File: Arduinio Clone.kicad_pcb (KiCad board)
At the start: 2 copper layers, 0 parts

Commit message: Added design rules
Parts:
- added BT1: Battery 3V, Connector_PinHeader_2.54mm:PinHeader_1x02_P2.54mm_Vertical, F.Cu at (130.8, 66.0)
- added C1: 220pF, Capacitor_SMD:C_0805_2012Metric, F.Cu at (127.7, 79.5)
- added C2: 220pF, Capacitor_SMD:C_0805_2012Metric, F.Cu at (133.4, 72.4)
- added C3: 10uF, Capacitor_SMD:C_0805_2012Metric, F.Cu at (140.4, 65.2)
- added D1: LED, LED_SMD:LED_0805_2012Metric, F.Cu at (128.9, 72.4)
- added J1: Serial, Connector_PinHeader_2.54mm:PinHeader_1x04_P2.54mm_Vertical, F.Cu at (157.3, 66.0)
- added J2: Digital Pins, Connector_PinHeader_2.54mm:PinHeader_1x09_P2.54mm_Vertical, F.Cu at (148.0, 66.0)
- added J3: ICSP, Connector_PinHeader_2.54mm:PinHeader_2x03_P2.54mm_Vertical, F.Cu at (161.9, 66.0)
- added J4: I2C, Connector_PinHeader_2.54mm:PinHeader_1x04_P2.54mm_Vertical, F.Cu at (152.6, 66.0)
- added R1: 330, Resistor_SMD:R_0805_2012Metric_Pad1.20x1.40mm_HandSolder, F.Cu at (127.9, 76.5)
- added R2: 10k, Resistor_SMD:R_0805_2012Metric_Pad1.20x1.40mm_HandSolder, F.Cu at (135.5, 68.6)
- added U1: DS1337_GM, Package_SO:SO-8_5.3x6.2mm_P1.27mm, F.Cu at (111.8, 79.2)
- added U2: 24LC1025, Package_SO:SOIC-8_3.9x4.9mm_P1.27mm, F.Cu at (122.5, 71.8)
- added U3: ATmega328P-A, Package_QFP:TQFP-32_7x7mm_P0.8mm, F.Cu at (112.4, 69.5)
- added U4: 24LC1025, Package_SO:SOIC-8_3.9x4.9mm_P1.27mm, F.Cu at (121.3, 78.6)
- added Y1: Crystal 32MHz, Crystal:Crystal_SMD_MicroCrystal_CC7V-T1A-2Pin_3.2x1.5mm, F.Cu at (135.7, 65.4)
- added Y2: Crystal 16MHz, Crystal:Crystal_SMD_5032-2Pin_5.0x3.2mm_HandSoldering, F.Cu at (123.4, 66.1)

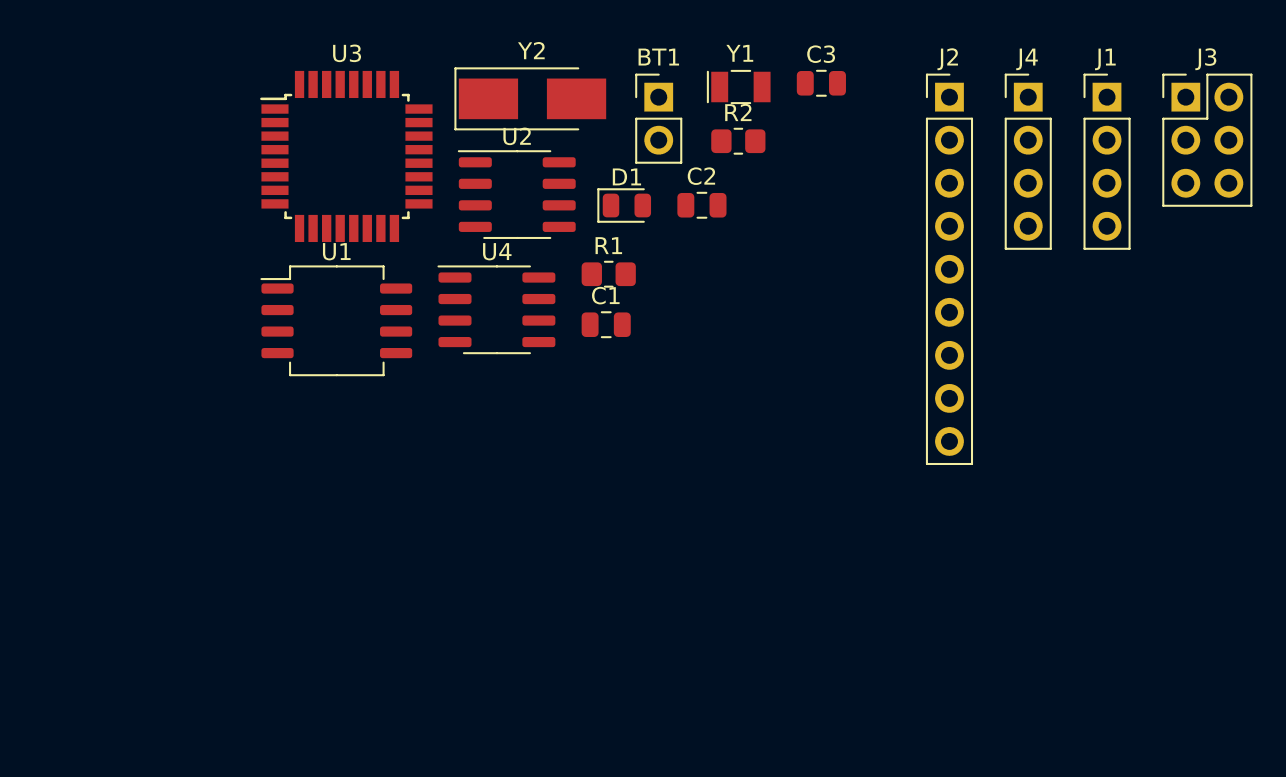
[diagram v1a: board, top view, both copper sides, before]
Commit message: Component placement in PCB
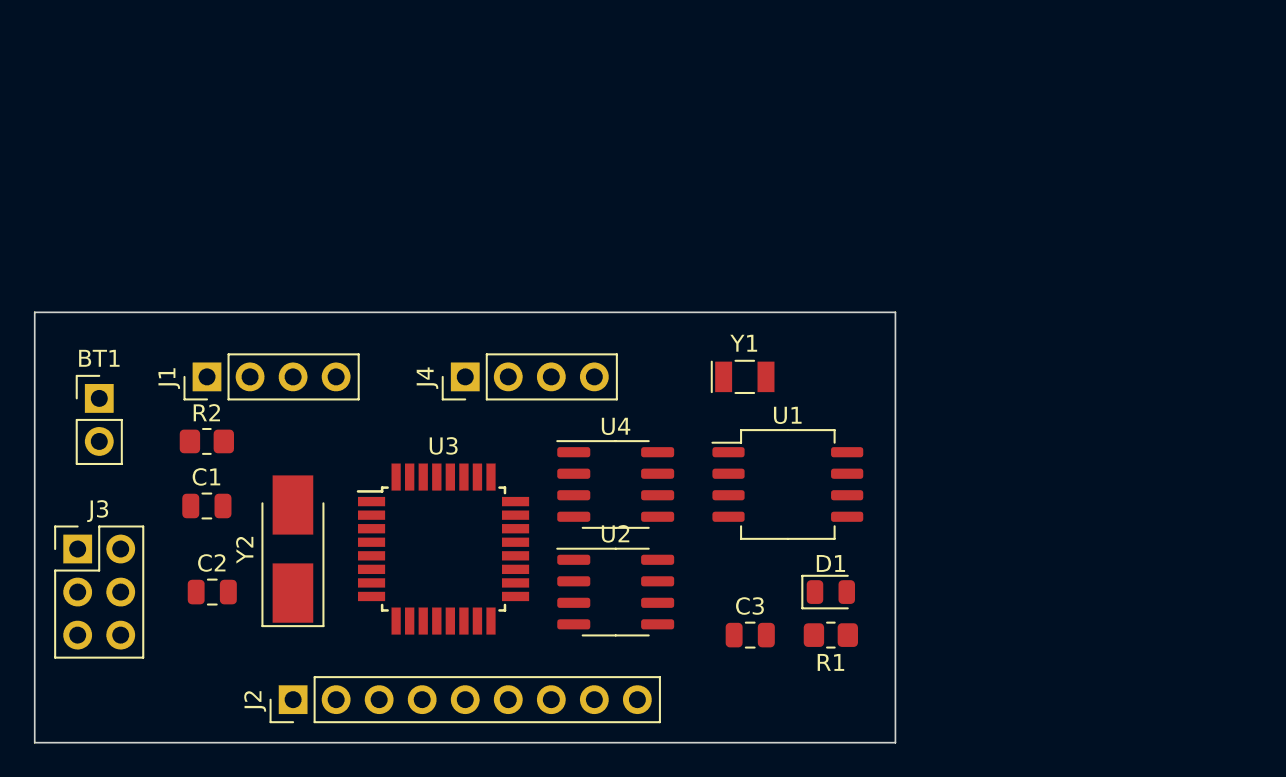
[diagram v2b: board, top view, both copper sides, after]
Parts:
- moved J3 70.6 mm to (96.5, 92.7)
- moved J1 55.6 mm to (104.2, 82.5), turned to 90 degrees
- moved J2 52.6 mm to (109.2, 101.6), turned to 90 degrees
- moved BT1 37.5 mm to (97.8, 83.8)
- moved J4 37.1 mm to (119.4, 82.5), turned to 90 degrees
- moved C2 36.8 mm to (104.5, 95.2)
- moved R2 36.0 mm to (104.1, 86.4)
- moved C3 32.8 mm to (136.2, 97.8)
- moved Y2 30.1 mm to (109.2, 92.7), turned to 90 degrees
- moved U1 28.3 mm to (138.4, 88.9)
- moved C1 25.9 mm to (104.1, 90.2)
- moved D1 25.8 mm to (141.0, 95.2)
- moved R1 25.0 mm to (141.0, 97.8), turned to 180 degrees
- moved U2 24.2 mm to (128.3, 95.2)
- moved U3 23.9 mm to (118.1, 92.7)
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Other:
- board outline added: 50.8 x 25.4 mm

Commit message: Made edge cuts
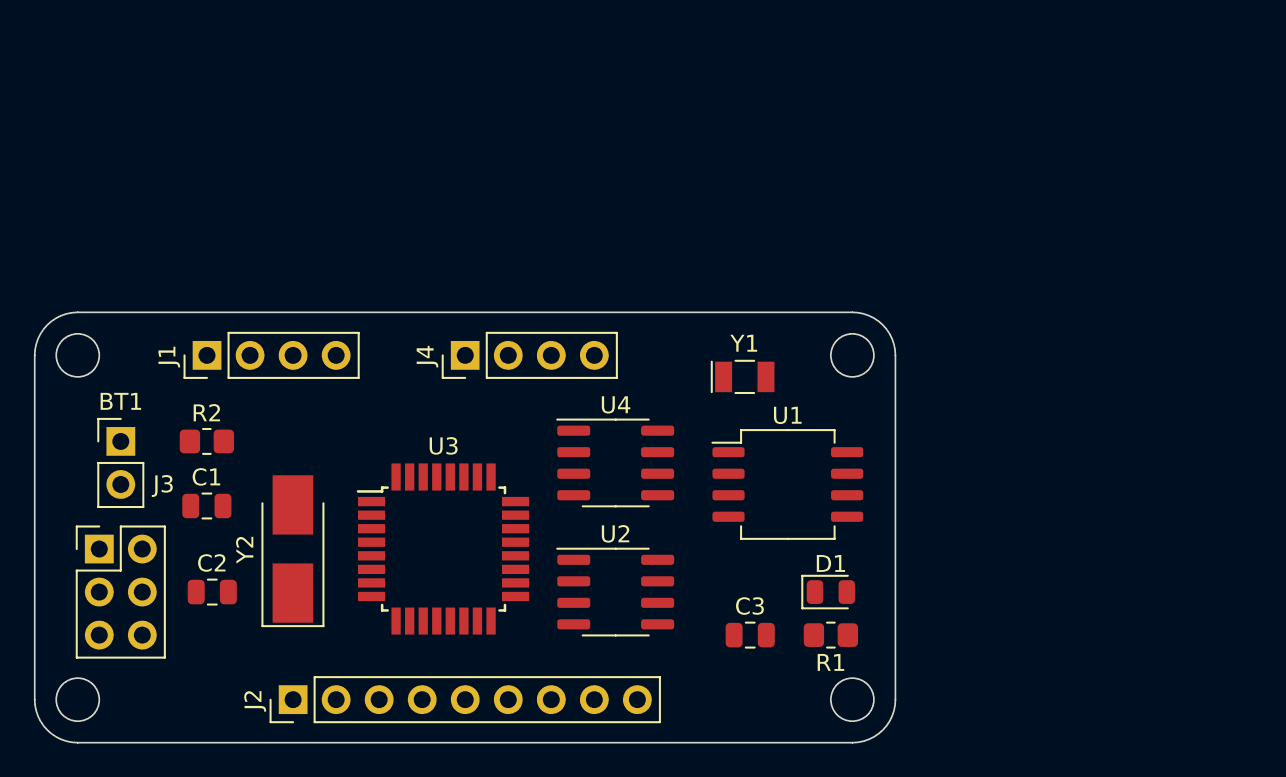
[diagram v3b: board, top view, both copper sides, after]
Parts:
- moved BT1 2.84 mm to (99.1, 86.4)
- moved J3 1.28 mm to (97.8, 92.7)
- moved U4 1.27 mm to (128.3, 87.6)
- moved J1 1.27 mm to (104.2, 81.3)
- moved J4 1.27 mm to (119.4, 81.3)
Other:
- outline, holes or cut-outs redrawn
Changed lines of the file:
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@@
     )
     (pad_to_mask_clearance 0)
+    (aux_axis_origin 142.983948 102.343948)
     (pcbplotparams
       (layerselection 0x00010fc_ffffffff)
@@
   )
   (footprint "Connector_PinHeader_2.54mm:PinHeader_1x04_P2.54mm_Vertical" (layer "F.Cu")
-    (at 104.15 82.55 90)
+    (at 104.15 81.28 90)
     (descr "Through hole straight pin header, 1x04, 2.54mm pitch, single row")
     (tags "Through hole pin header THT 1x04 2.54mm single row")
@@
   )
   (footprint "Connector_PinHeader_2.54mm:PinHeader_2x03_P2.54mm_Vertical" (layer "F.Cu")
-    (at 96.515 92.71)
+    (at 97.79 92.71)
     (descr "Through hole straight pin header, 2x03, 2.54mm pitch, double rows")
     (tags "Through hole pin header THT 2x03 2.54mm double row")
@@
     (property "Sheetname" "Connectors")
     (attr through_hole)
-    (fp_text reference "J3" (at 1.27 -2.33) (layer "F.SilkS")
+    (fp_text reference "J3" (at 3.81 -3.81) (layer "F.SilkS")
       (effects (font (size 1 1) (thickness 0.15)))
     )
@@
       (effects (font (size 1 1) (thickness 0.15)))
     )
-    (fp_text value "Digital Pins" (at 0 22.65 90) (layer "F.Fab")
+    (fp_text value "Digital Pins" (at -1.27 26.66 180) (layer "F.Fab")
       (effects (font (size 1 1) (thickness 0.15)))
     )
@@
   )
   (footprint "Connector_PinHeader_2.54mm:PinHeader_1x02_P2.54mm_Vertical" (layer "F.Cu")
-    (at 97.79 83.82)
+    (at 99.06 86.36)
     (descr "Through hole straight pin header, 1x02, 2.54mm pitch, single row")
     (tags "Through hole pin header THT 1x02 2.54mm single row")
@@
   )
   (footprint "Connector_PinHeader_2.54mm:PinHeader_1x04_P2.54mm_Vertical" (layer "F.Cu")
-    (at 119.39 82.55 90)
+    (at 119.39 81.28 90)
     (descr "Through hole straight pin header, 1x04, 2.54mm pitch, single row")
     (tags "Through hole pin header THT 1x04 2.54mm single row")
@@
   )
   (footprint "Package_SO:SOIC-8_3.9x4.9mm_P1.27mm" (layer "F.Cu")
-    (at 128.27 88.9)
+    (at 128.27 87.63)
     (descr "SOIC, 8 Pin (JEDEC MS-012AA, https://www.analog.com/media/en/package-pcb-resources/package/pkg_pdf/soic_narrow-r/r_8.pdf), generated with kicad-footprint-generator ipc_gullwing_generator.py")
     (tags "SOIC SO")
@@
     )
   )
-  (gr_rect (start 93.98 78.74) (end 144.78 104.14) (layer "Edge.Cuts") (width 0.1) (fill none))
+  (gr_circle (center 142.24 101.6) (end 142.24 102.87) (layer "Edge.Cuts") (width 0.1) (fill none))
+  (gr_circle (center 96.520001 81.280001) (end 96.520001 82.550001) (layer "Edge.Cuts") (width 0.1) (fill none))
+  (gr_line (start 93.98 81.28) (end 93.98 101.6) (layer "Edge.Cuts") (width 0.1))
+  (gr_arc (start 93.98 81.28) (mid 94.723949 79.483949) (end 96.52 78.74) (layer "Edge.Cuts") (width 0.1))
+  (gr_arc (start 142.240001 78.739999) (mid 144.036052 79.483948) (end 144.780001 81.279999) (layer "Edge.Cuts") (width 0.1))
+  (gr_arc (start 93.98 104.14) (mid 93.98 104.14) (end 93.98 104.14) (layer "Edge.Cuts") (width 0.1))
+  (gr_line (start 142.240001 78.739999) (end 96.52 78.74) (layer "Edge.Cuts") (width 0.1))
+  (gr_line (start 144.780001 101.600001) (end 144.780001 81.279999) (layer "Edge.Cuts") (width 0.1))
+  (gr_arc (start 96.52 104.14) (mid 94.723949 103.396051) (end 93.98 101.6) (layer "Edge.Cuts") (width 0.1))
+  (gr_line (start 96.52 104.14) (end 142.240001 104.140001) (layer "Edge.Cuts") (width 0.1))
+  (gr_circle (center 96.52 101.6) (end 96.52 102.87) (layer "Edge.Cuts") (width 0.1) (fill none))
+  (gr_circle (center 142.24 81.28) (end 142.24 82.55) (layer "Edge.Cuts") (width 0.1) (fill none))
+  (gr_arc (start 144.780001 101.600001) (mid 144.036052 103.396052) (end 142.240001 104.140001) (layer "Edge.Cuts") (width 0.1))
 )

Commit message: Imported generated Spectra sessionfile and ran DRC
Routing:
- net GNDPWR: track 0.00 -> 141.7 mm
- net /VCC: track 0.00 -> 111.9 mm
- net /SCK: track 0.00 -> 104.9 mm
- net /SDA: track 0.00 -> 49.0 mm, vias 0 -> 2
- net /MISO: track 0.00 -> 43.2 mm
- net /RESET: track 0.00 -> 41.5 mm
- net /ADDR2: track 0.00 -> 21.6 mm
- net /D2: track 0.00 -> 21.4 mm, vias 0 -> 1
- net /MOSI: track 0.00 -> 21.3 mm, vias 0 -> 1
- net /D3: track 0.00 -> 16.6 mm, vias 0 -> 1
- net /D4: track 0.00 -> 14.9 mm, vias 0 -> 1
- net /RX: track 0.00 -> 14.1 mm
- net Net-(C1-Pad2): track 0.00 -> 11.9 mm
- net /ADDR1: track 0.00 -> 10.9 mm
- net /D8: track 0.00 -> 9.56 mm
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
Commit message: Saved fully routed 4 layer board
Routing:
- net /VCC: track 111.9 -> 139.7 mm
- net /SCK: track 104.9 -> 84.5 mm, vias 0 -> 1
- net GNDPWR: track 141.7 -> 128.8 mm, vias 0 -> 1
- net /RESET: track 41.5 -> 33.5 mm
- net /D2: track 21.4 -> 27.4 mm, vias 1 -> 0
- net /MOSI: track 21.3 -> 27.1 mm
- net Net-(U1-Pad1): track 5.36 -> 10.0 mm
- net /D3: track 16.6 -> 13.4 mm
- net /SDA: track 49.0 -> 46.3 mm
- net /D4: track 14.9 -> 12.8 mm
- net /RX: track 14.1 -> 12.6 mm, vias 0 -> 1
- net /D6: track 6.55 -> 6.00 mm
- net /TX: vias 0 -> 1
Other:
- copper layers 2 -> 4
